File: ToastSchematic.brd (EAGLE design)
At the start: 90 x 75 mm, 83 parts, among them Q1 DMN63D8LDW, Q2 DMN63D8LDW, Q3 DMN63D8LDW, Q4 DMN63D8LDW, T1 BPX81, T2 BPX81, T3 BPX81, T4 BPX81, T5 BPX81, T6 BPX81, U3 DRV8839_DSS_12, U4 DRV8839_DSS_12

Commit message: added gnd plane
added gnd plane
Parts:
- moved R17 28.2 mm to (38.8, 43.0)
- moved SPK1 24.9 mm to (39.2, 38.2)
- moved C_BUZ 18.9 mm to (36.4, 33.7)
- moved R12 10.8 mm to (60.9, 29.9), turned to 90 degrees
- moved Q3 9.47 mm to (67.2, 23.4), turned to 270 degrees
- moved C17 6.38 mm to (71.4, 24.0)
- moved C16 5.71 mm to (74.3, 35.9)
- moved U$7 4.75 mm to (65.3, 29.7)
- moved C_IMU2 4.04 mm to (70.0, 30.7)
- moved C_IMU 3.05 mm to (70.0, 27.4)
- moved C_IMU3 3.01 mm to (70.0, 29.1)
- moved S1 2.25 mm to (6.20, 23.1)
- moved R21 2.02 mm to (71.2, 22.1)
- moved R20 1.77 mm to (74.5, 33.8)
- moved C_VCAP 1.52 mm to (59.2, 38.3)
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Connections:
- net DGND: now also U$4.L_GND, U$4.R_GND
- net GND: no longer U$4.L_GND, U$4.R_GND
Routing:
- added copper zone on layer 16, net AGND
- added copper zone on layer 16, net GND

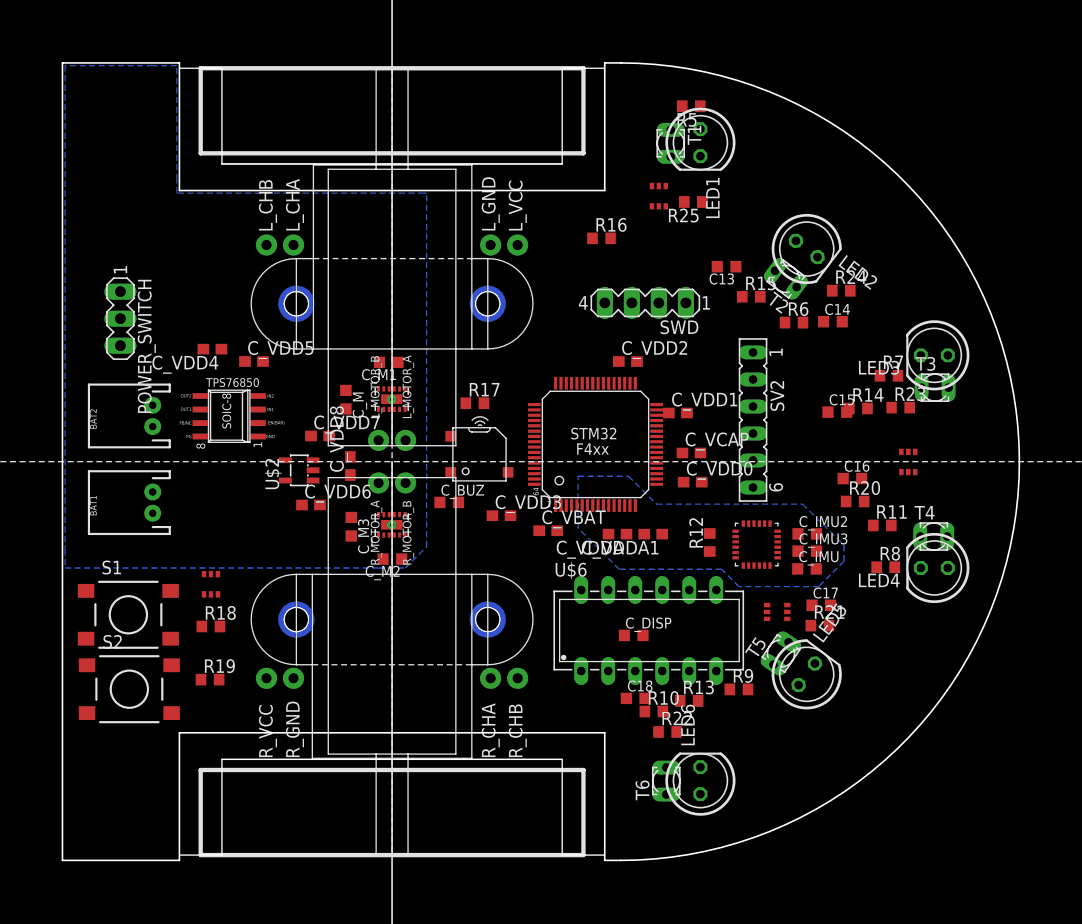
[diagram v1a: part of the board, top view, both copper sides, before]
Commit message: did dgnd, agnd, and gnd planes
added some traces, still need to add all the power planes
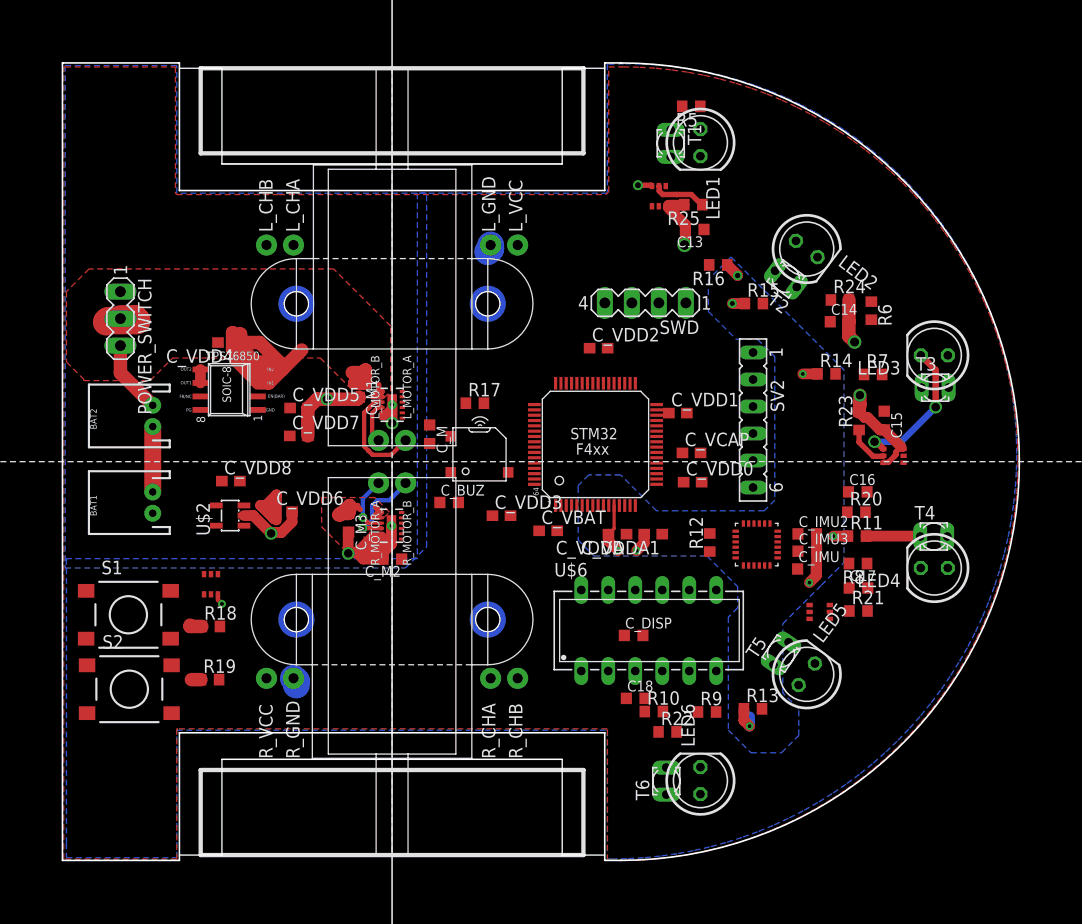
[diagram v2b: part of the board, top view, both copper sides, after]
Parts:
- moved C_VDD8 11.3 mm to (15.8, 35.7), turned to 0 degrees
- moved R16 11.3 mm to (61.7, 56.0), turned to 180 degrees
- moved C_M 8.52 mm to (34.5, 40.1)
- moved U$2 7.77 mm to (15.8, 32.4)
- moved R6 7.37 mm to (76.1, 51.7), turned to 270 degrees
- moved C_VDD5 6.10 mm to (22.3, 42.5)
- moved R13 6.05 mm to (64.9, 14.2)
- moved C13 4.61 mm to (59.5, 59.3)
- moved C15 4.48 mm to (77.3, 41.4), turned to 270 degrees
- moved R14 4.42 mm to (71.9, 45.8)
- moved R23 4.10 mm to (74.9, 41.3), turned to 90 degrees
- moved Q3 4.00 mm to (71.2, 23.4)
- moved R21 3.88 mm to (74.9, 23.5)
- moved C17 3.86 mm to (74.9, 25.6)
- moved R9 3.68 mm to (60.6, 14.0)
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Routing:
- net V_BATT: track 0.00 -> 43.9 mm
- net GND: track 0.00 -> 41.7 mm, vias 0 -> 4
- net DGND: track 0.00 -> 25.0 mm, vias 0 -> 5
- net AGND: track 0.00 -> 19.6 mm, vias 0 -> 8
- net N$23: track 0.00 -> 13.7 mm, vias 0 -> 2
- net MOTOR_LEFT_1: track 0.00 -> 10.1 mm
- net +3V3: track 0.00 -> 8.84 mm
- net MOTOR_RIGHT_2: track 0.00 -> 8.38 mm, vias 0 -> 1
- net N$2: track 0.00 -> 6.87 mm
- net N$1: track 0.00 -> 6.15 mm
- net MOTOR_RIGHT_1: track 0.00 -> 5.81 mm, vias 0 -> 1
- net REC_FR: track 0.00 -> 5.12 mm
- net IR_L: track 0.00 -> 5.07 mm
- net IR_FL: track 0.00 -> 4.01 mm
- net MOTOR_LEFT_2: track 0.00 -> 3.96 mm
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- added copper zone on layer 1, net +3V3
- added copper zone on layer 16, net DGND
- added copper zone on layer 1, net V_BATT

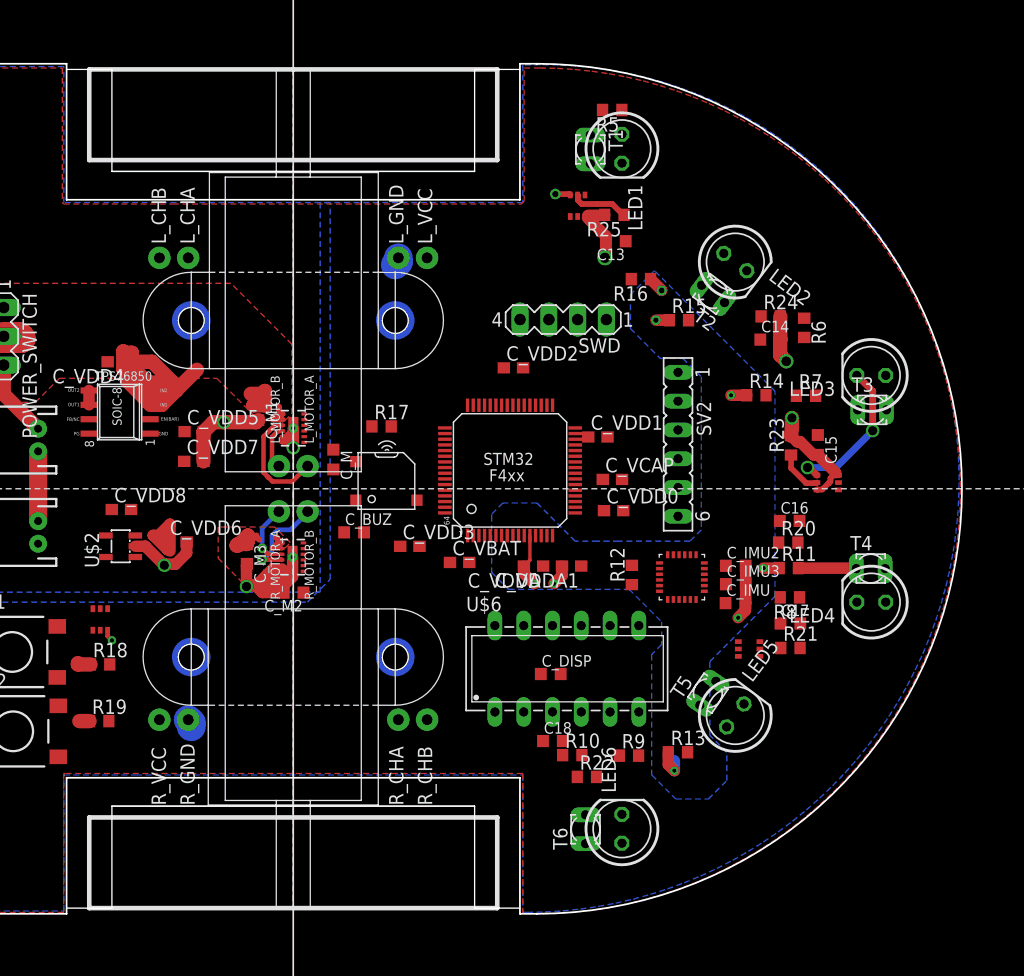
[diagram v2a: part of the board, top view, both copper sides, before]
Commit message: added 5V plane
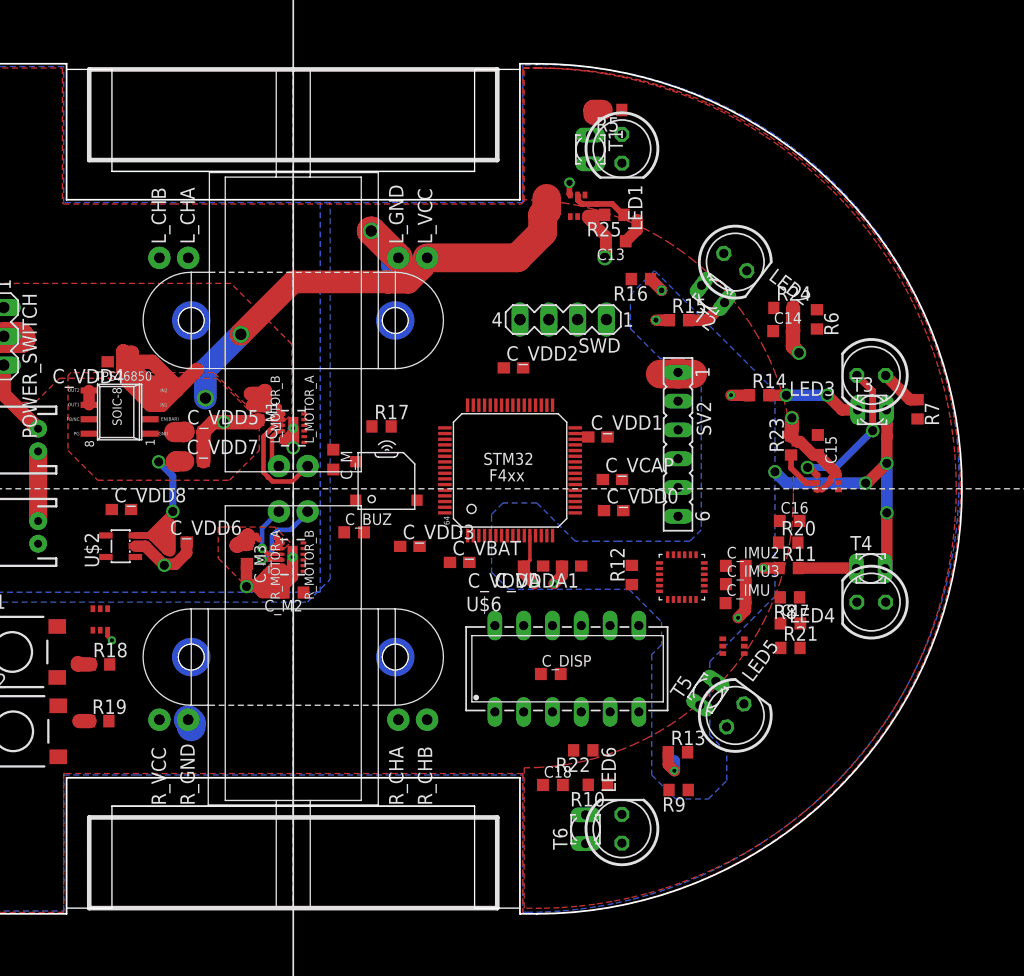
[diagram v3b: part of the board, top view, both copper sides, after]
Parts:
- moved R7 9.91 mm to (86.1, 44.5), turned to 270 degrees
- moved R9 5.33 mm to (65.0, 10.9), turned to 180 degrees
- moved C18 3.88 mm to (53.9, 11.4)
- moved R10 3.46 mm to (57.9, 11.4), turned to 180 degrees
- moved R22 2.36 mm to (56.6, 14.4), turned to 180 degrees
- moved Q3 1.40 mm to (69.8, 23.6)
- moved C14 1.35 mm to (74.2, 51.4)
- moved R24 1.35 mm to (74.2, 53.5)
- moved R6 1.35 mm to (77.2, 52.5)
- moved R14 0.25 mm to (72.1, 45.8)
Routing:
- net +5V: track 1.27 -> 56.3 mm, vias 0 -> 4
- net +3V3: track 8.84 -> 36.9 mm, vias 0 -> 4
- net REC_FL: track 0.00 -> 8.37 mm, vias 0 -> 2
- net REC_DL: track 0.00 -> 3.82 mm
- net N$20: track 0.00 -> 3.70 mm
- net DGND: track 25.0 -> 28.1 mm, vias 5 -> 6
- added copper zone on layer 1, net +5V

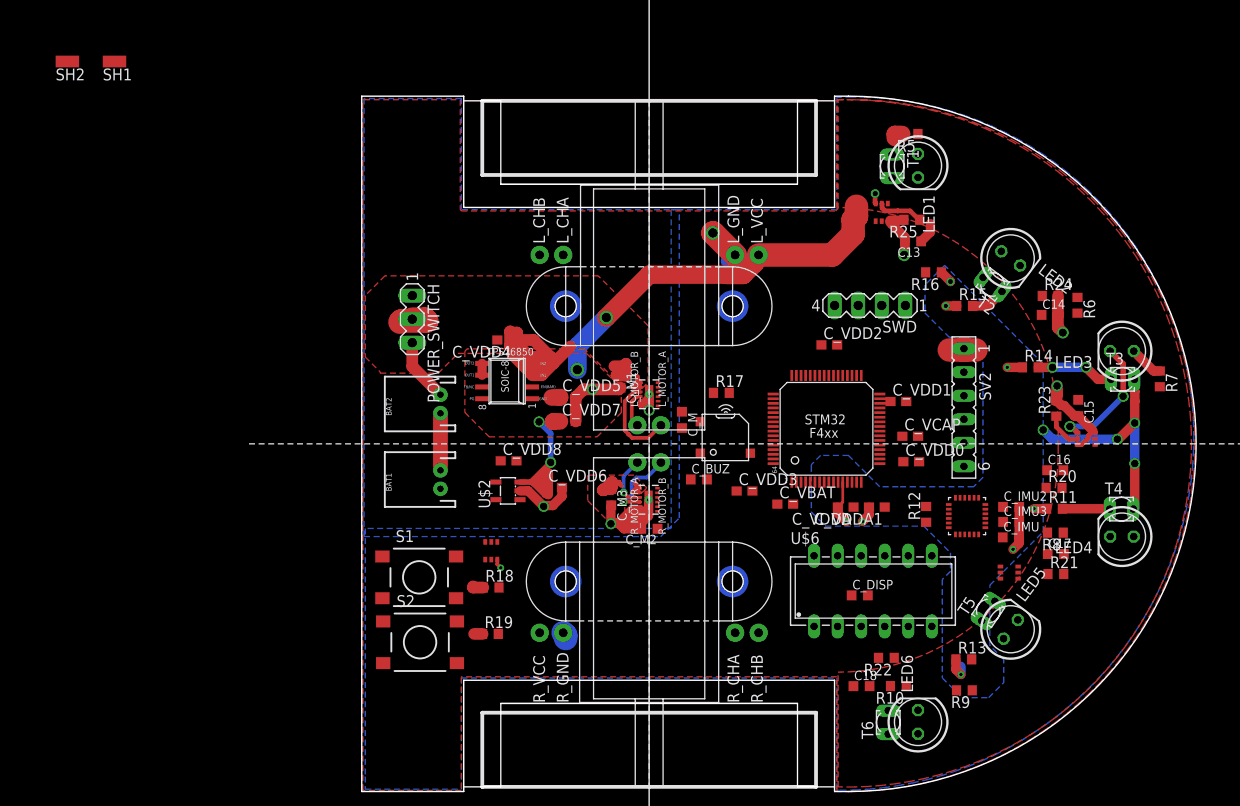
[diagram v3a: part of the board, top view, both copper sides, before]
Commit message: some routing
Partially routed IRs and other stuff
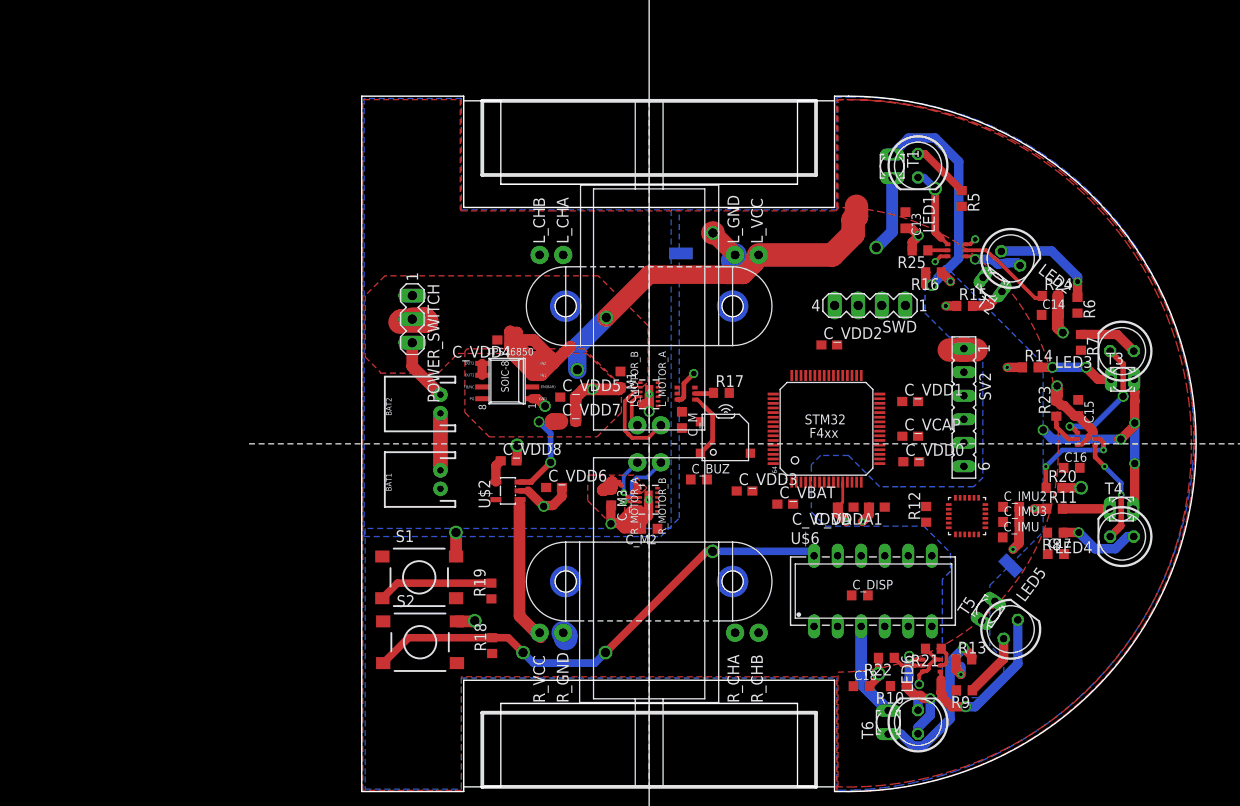
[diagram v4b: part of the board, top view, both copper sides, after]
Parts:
- moved SH2 115.3 mm to (70.0, 24.4), flipped to the bottom, turned to 225 degrees
- moved SH1 64.5 mm to (34.4, 58.0), flipped to the bottom
- moved Q4 27.0 mm to (35.0, 42.9), turned to 270 degrees
- moved R21 15.5 mm to (61.7, 15.4), turned to 180 degrees
- moved Q3 13.1 mm to (61.5, 13.6)
- moved R7 9.38 mm to (77.6, 48.4)
- moved Q1 9.04 mm to (64.1, 58.4), turned to 90 degrees
- moved R5 8.91 mm to (64.7, 64.0), turned to 270 degrees
- moved R18 6.26 mm to (14.1, 15.7), turned to 90 degrees
- moved R19 4.63 mm to (14.0, 21.6), turned to 90 degrees
- moved R25 3.42 mm to (60.2, 58.4)
- moved C13 2.42 mm to (58.6, 61.6), turned to 270 degrees
- moved C16 1.80 mm to (76.6, 34.9)
- moved C_VDD1 1.27 mm to (59.1, 42.1)
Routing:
- net NRST: track 0.00 -> 53.9 mm, vias 0 -> 3
- net REC_L: track 0.00 -> 25.6 mm, vias 0 -> 1
- net REC_R: track 0.00 -> 18.3 mm, vias 0 -> 1
- net N$25: track 0.00 -> 18.1 mm, vias 0 -> 1
- net DGND: track 28.1 -> 45.1 mm, vias 6 -> 12
- net BTN1: track 0.00 -> 12.4 mm
- net N$21: track 0.00 -> 11.6 mm, vias 0 -> 1
- net N$24: track 0.00 -> 11.6 mm, vias 0 -> 2
- net +5V: track 56.3 -> 67.7 mm
- net IR_FR: track 0.00 -> 11.1 mm, vias 0 -> 2
- net IR_DL: track 0.00 -> 10.5 mm
- net +3V3: track 36.9 -> 47.0 mm, vias 4 -> 5
- net N$16: track 0.00 -> 8.94 mm, vias 0 -> 1
- net N$14: track 0.00 -> 8.88 mm, vias 0 -> 1
- net N$26: track 0.00 -> 7.93 mm, vias 0 -> 1
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
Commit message: Restarted routing
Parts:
- moved R17 29.4 mm to (51.3, 16.4), turned to 90 degrees
- moved Q4 28.4 mm to (49.0, 18.2), turned to 0 degrees
- moved C_BUZ 21.3 mm to (52.2, 19.4), turned to 180 degrees
- moved C_DISP 19.4 mm to (44.4, 38.2), turned to 270 degrees
- moved U$6 19.2 mm to (44.4, 37.5), turned to 270 degrees
- moved SPK1 18.9 mm to (50.3, 22.8)
- moved C_IMU3 17.0 mm to (54.4, 22.6), turned to 270 degrees
- moved C_IMU2 16.1 mm to (56.0, 22.7), turned to 270 degrees
- moved SV2 14.7 mm to (53.7, 50.9), flipped to the bottom, turned to 180 degrees
- moved R16 14.3 mm to (53.7, 67.9), turned to 90 degrees
- moved R13 13.2 mm to (53.6, 7.45), turned to 270 degrees
- moved C17 12.4 mm to (71.2, 13.8), turned to 90 degrees
- moved C16 11.6 mm to (85.3, 27.3), turned to 270 degrees
- moved C_VCAP 10.9 mm to (69.4, 41.9)
- moved R8 10.7 mm to (85.2, 30.7), turned to 90 degrees
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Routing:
- net +5V: track 67.7 -> 0.00 mm, vias 4 -> 0
- net NRST: track 53.9 -> 0.00 mm, vias 3 -> 0
- net +3V3: track 47.0 -> 0.00 mm, vias 5 -> 0
- net GND: track 45.4 -> 0.00 mm, vias 6 -> 0
- net DGND: track 45.1 -> 0.00 mm, vias 12 -> 0
- net V_BATT: track 37.1 -> 0.00 mm
- net REC_L: track 25.6 -> 0.00 mm, vias 1 -> 0
- net AGND: track 19.9 -> 0.00 mm, vias 8 -> 0
- net REC_R: track 18.3 -> 0.00 mm, vias 1 -> 0
- net N$25: track 18.1 -> 0.00 mm, vias 1 -> 0
- net N$23: track 13.7 -> 0.00 mm, vias 2 -> 0
- net BTN1: track 12.4 -> 0.00 mm
- net N$21: track 11.6 -> 0.00 mm, vias 1 -> 0
- net N$24: track 11.6 -> 0.00 mm, vias 2 -> 0
- net IR_FR: track 11.1 -> 0.00 mm, vias 2 -> 0
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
